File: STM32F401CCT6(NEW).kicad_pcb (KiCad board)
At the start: 2 copper layers, 37 parts, among them J1 USB_OTG, J2 Conn_02x03_Odd_Even, J3 Conn_01x20_des, J4 Conn_01x05_desc, J5 Conn_01x20, SW1 SW_Push, U1 MIC5219-3.3, U2 STM32F401CCT6, U3 USBLC6-2SC6, Y1 32.786K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

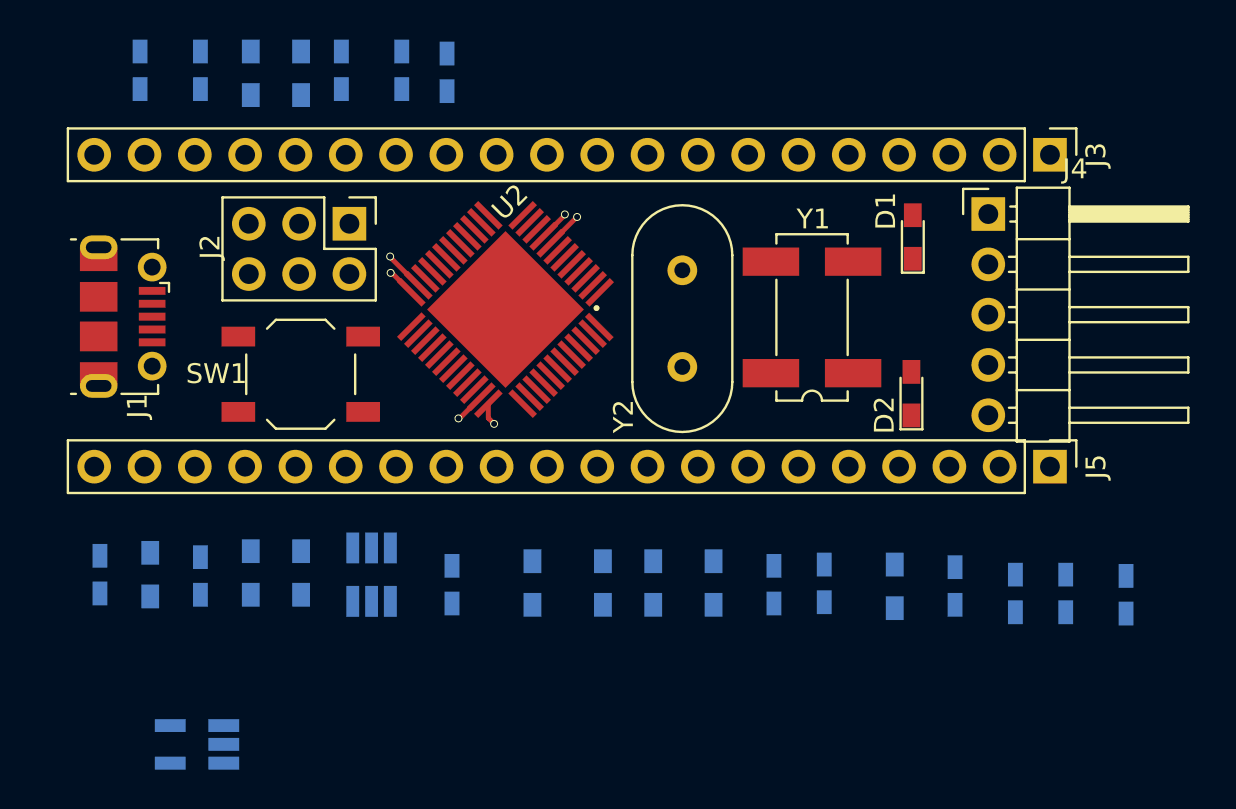
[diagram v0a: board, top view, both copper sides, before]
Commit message: Fixed QFPN48 pin 47 and 48 distances to 0.2
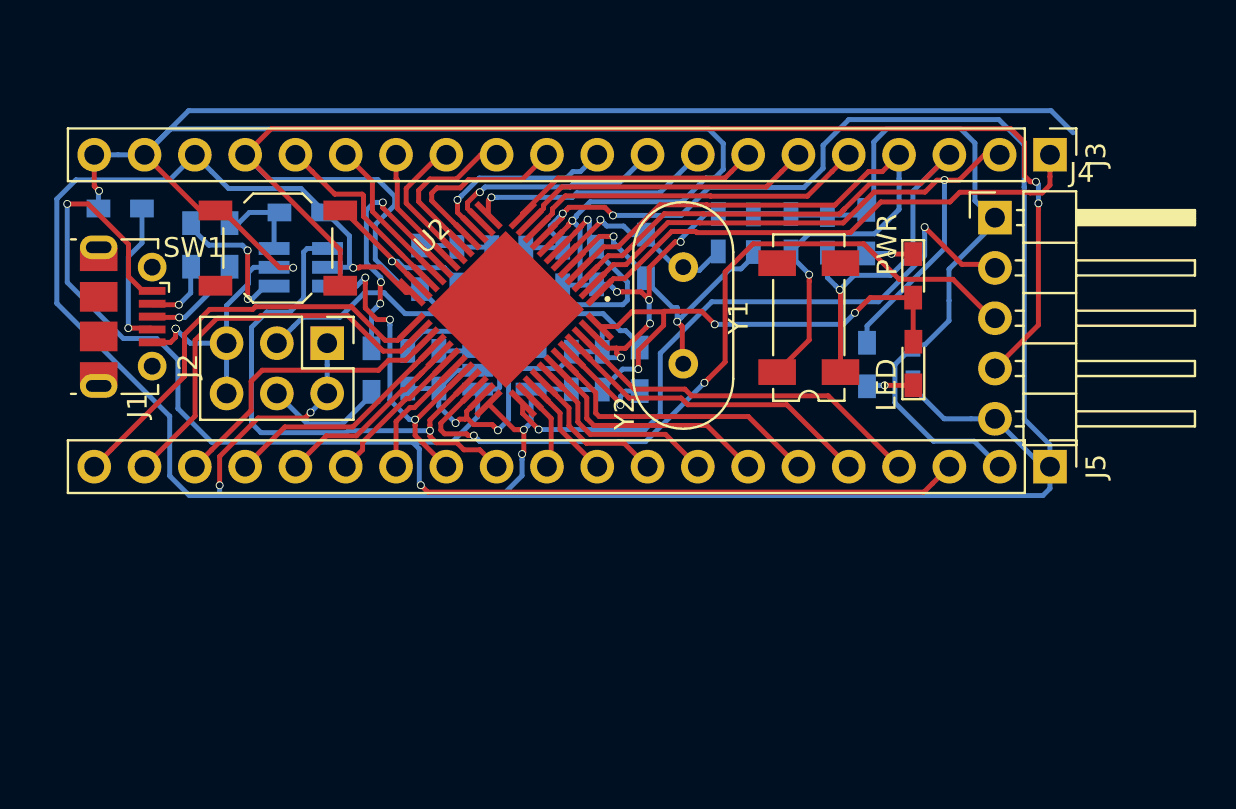
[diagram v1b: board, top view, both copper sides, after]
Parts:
- U2: footprint UFQFPN48:UFQFPN48 -> QFPN48:UFQFPN48
- Y1: footprint Crystals:Crystal_SMD_SeikoEpson_MC306-4pin_8.0x3.2mm_HandSoldering -> Crystals:Crystal_SMD_SeikoEpson_MC306-4pin_8.0x3.2mm
- moved C14 42.4 mm to (117.4, 114.2), turned to 90 degrees
- moved R6 34.4 mm to (115.1, 114.2)
- moved C2 32.7 mm to (91.9, 114.5)
- moved C8 32.0 mm to (109.3, 107.6)
- moved R5 29.6 mm to (115.0, 107.5), turned to 270 degrees
- moved R10 28.0 mm to (86.5, 106.5), turned to 0 degrees
- moved C9 27.4 mm to (107.6, 107.6), turned to 90 degrees
- moved R4 27.4 mm to (82.9, 108.2)
- moved C4 26.0 mm to (101.7, 114.5)
- moved C3 25.4 mm to (101.4, 109.2), turned to 270 degrees
- moved U1 24.4 mm to (96.8, 114.5), turned to 0 degrees
- moved C6 23.7 mm to (113.1, 107.6), turned to 90 degrees
- moved C5 22.2 mm to (100.2, 114.5), turned to 90 degrees
- moved C7 21.3 mm to (111.2, 107.6)
- moved R2 20.9 mm to (103.9, 108.8)
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- renumbered D2 to LED, D1 to PWR
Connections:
- C14 pad 1: +5V -> VCC
- J4 pad 5: +5V -> VCC
- R6 pad 1: GND -> /PC13
- Y1 pad 2: /PC15 -> (no net)
- Y1 pad 4: (no net) -> /PC15
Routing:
- net GND: track 5.54 -> 214.9 mm, vias 3 -> 13
- net VCC: track 4.14 -> 199.3 mm, vias 3 -> 10
- net /RESET: track 0.00 -> 94.6 mm, vias 0 -> 3
- net +5V: track 0.00 -> 74.6 mm, vias 0 -> 2
- net /SWDIO: track 0.00 -> 39.0 mm, vias 0 -> 2
- net /PC14: track 0.00 -> 38.1 mm, vias 0 -> 1
- net /PC15: track 0.00 -> 35.6 mm, vias 0 -> 1
- net /PC13: track 0.00 -> 33.1 mm, vias 0 -> 1
- net /SWDCLK: track 0.00 -> 32.0 mm, vias 0 -> 2
- net /PA12: track 0.00 -> 28.4 mm, vias 0 -> 1
- net /VBAT: track 0.00 -> 26.6 mm
- net /PB12: track 0.00 -> 21.6 mm
- net Net-(J2-Pad3): track 0.00 -> 20.6 mm
- net /PB13: track 0.00 -> 20.3 mm
- net /PB9: track 0.00 -> 18.5 mm
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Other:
- net class Default: clearance 0.2 -> 0.19999
- net class new: clearance 0.2 -> 0.19999
- rule trace_clearance: 0.2 -> 0.19999

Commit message: Finish routing
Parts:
- removed the LED at (117.4, 114.2)
- removed the PWR at (117.4, 109.7)
- added LED: LED_ALT, LEDs:LED_0805_HandSoldering, F.Cu at (117.4, 114.1)
- added PWR: LED_ALT, LEDs:LED_0805_HandSoldering, F.Cu at (117.4, 108.6)
- moved J4 0.34 mm to (121.5, 106.5)
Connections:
- J1 pad 6: Net-(J1-Pad6) -> (no net)
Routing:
- net GND: track 214.9 -> 165.5 mm
- net VCC: track 199.3 -> 201.6 mm
- net Net-(D1-Pad1): track 2.42 -> 3.27 mm
- net /PC13: track 33.1 -> 33.9 mm
- added copper zone on B.Cu, net GND
- added copper zone on F.Cu, net GND
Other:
- board outline added: 52.8 x 22.1 mm
- board text added: "5V"
- board text added: "A0"
- board text added: "A1"
- board text added: "A10"
- board text added: "A11"
- board text added: "A12"
- board text added: "A15"
- board text added: "A2"
- board text added: "A3"
- board text added: "A4"
- board text added: "A5"
- board text added: "A6"
- board text added: "A7"
- board text added: "A8"
- board text added: "A9"
- board text added: "B0"
- board text added: "B1"
- board text added: "B10"
- board text added: "B11"
- board text added: "B12"
- board text added: "B13"
- board text added: "B14"
- board text added: "B15"
- board text added: "B3"
- board text added: "B4"
- board text added: "B5"
- board text added: "B6"
- board text added: "B7"
- board text added: "B8"
- board text added: "B9"
- board text added: "C13"
- board text added: "C14"
- board text added: "C15"
- board text added: "GND"
- board text added: "RST"
- board text added: "SWDCLK"
- board text added: "SWDIO"
- board text added: "VB"
- board text added: "VCC"

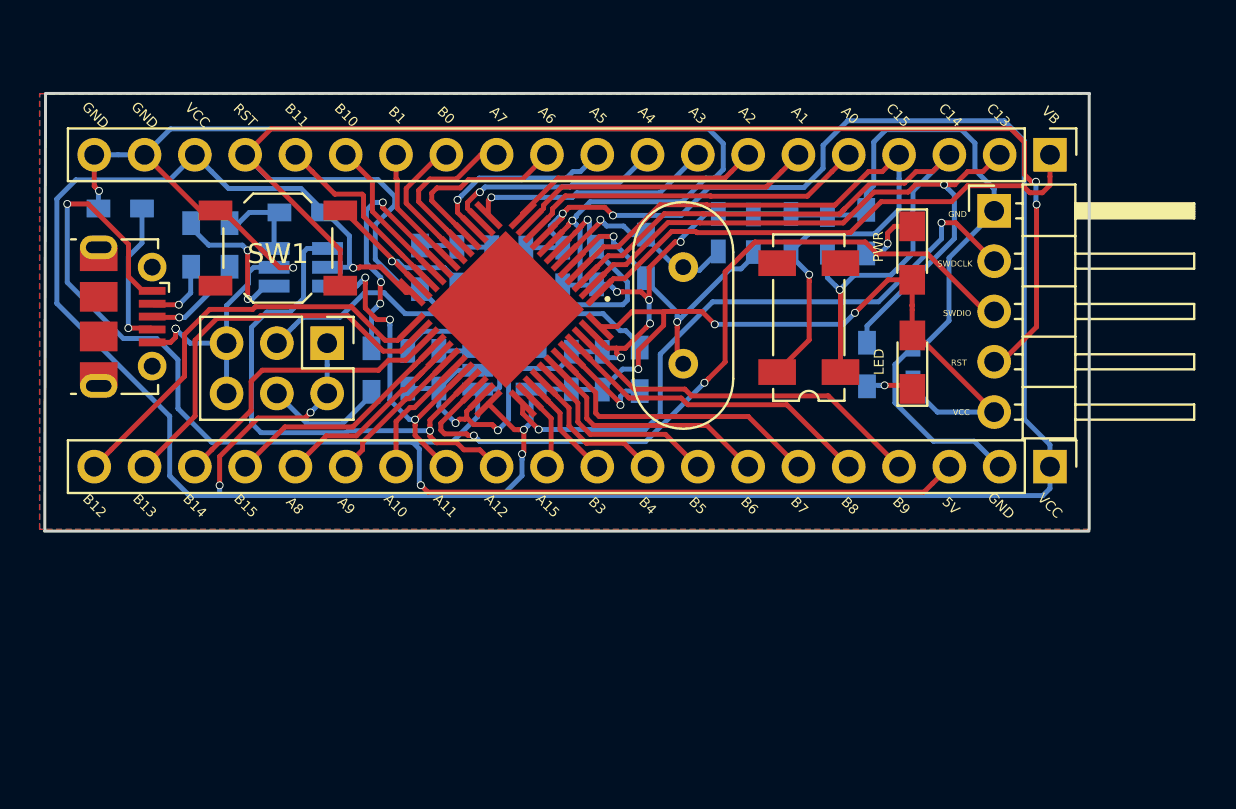
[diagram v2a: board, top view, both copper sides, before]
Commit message: Added pin name on silk layer
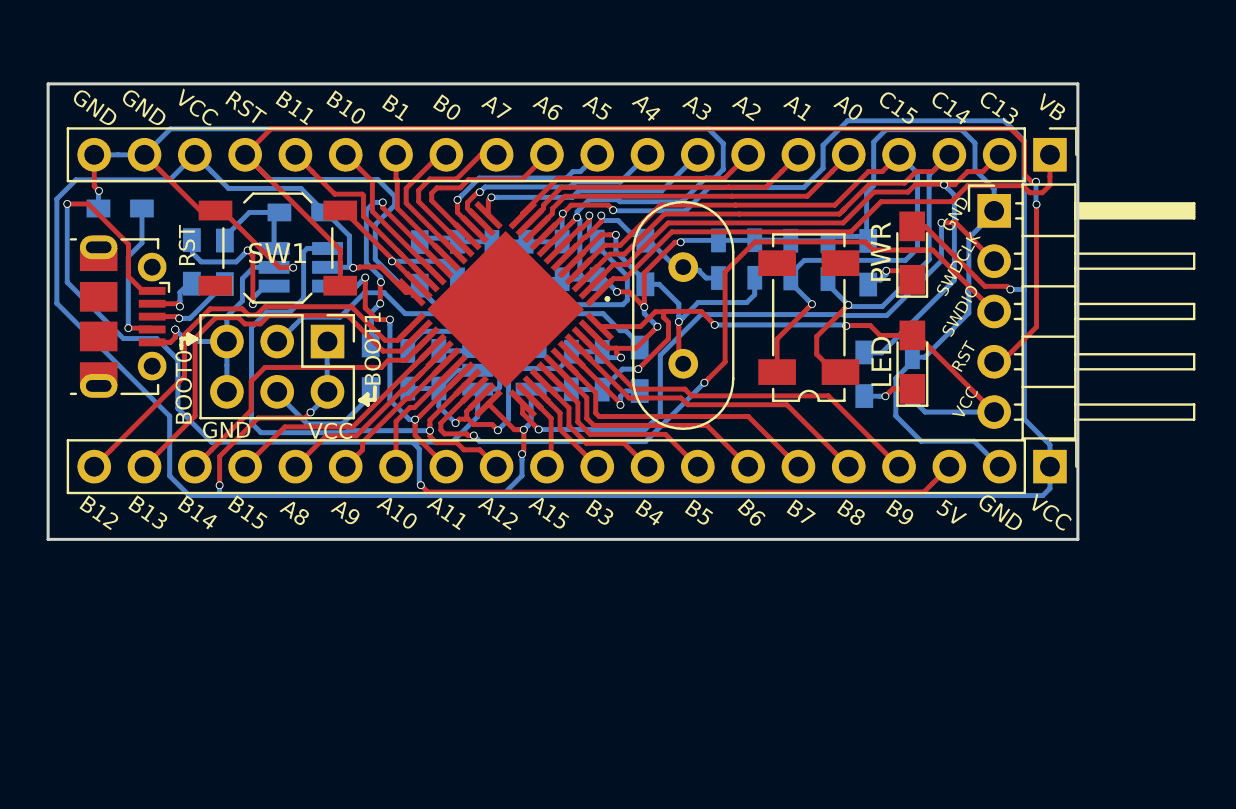
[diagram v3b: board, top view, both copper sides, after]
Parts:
- moved R5 1.57 mm to (115.1, 109.1)
- moved C7 1.36 mm to (111.2, 108.9)
- moved C9 1.34 mm to (107.6, 108.9)
- moved C6 1.33 mm to (113.1, 109.0)
- moved C8 1.30 mm to (109.4, 108.9)
- moved R4 0.91 mm to (82.7, 109.1)
- moved R3 0.86 mm to (81.0, 109.0)
- moved C14 0.63 mm to (117.4, 114.8)
- moved R6 0.51 mm to (114.9, 114.7)
- moved R2 0.31 mm to (103.9, 109.1)
- moved C11 0.31 mm to (99.7, 109.0)
- moved C10 0.29 mm to (97.9, 109.0)
- moved C3 0.26 mm to (101.5, 109.0)
- moved C12 0.26 mm to (94.4, 109.0)
- moved C13 0.26 mm to (96.1, 109.0)
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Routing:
- net GND: track 165.5 -> 168.4 mm
- net VCC: track 201.6 -> 204.5 mm, vias 10 -> 11
- net /PC15: track 35.6 -> 37.5 mm
- net /SWDIO: track 39.1 -> 41.0 mm
- net Net-(R3-Pad1): track 7.56 -> 8.51 mm
- net /PC13: track 33.9 -> 34.8 mm
- net /PC14: track 38.1 -> 38.8 mm
- net /SWDCLK: track 32.3 -> 32.9 mm
- net /OSCIN: track 16.8 -> 17.3 mm
- net /RESET: track 94.5 -> 95.0 mm
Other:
- board size 52.8 x 22.1 mm -> 52 x 23 mm
- board text added: "BOOT0"
- board text added: "BOOT1"

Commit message: Finish design the layout-Added Image on it
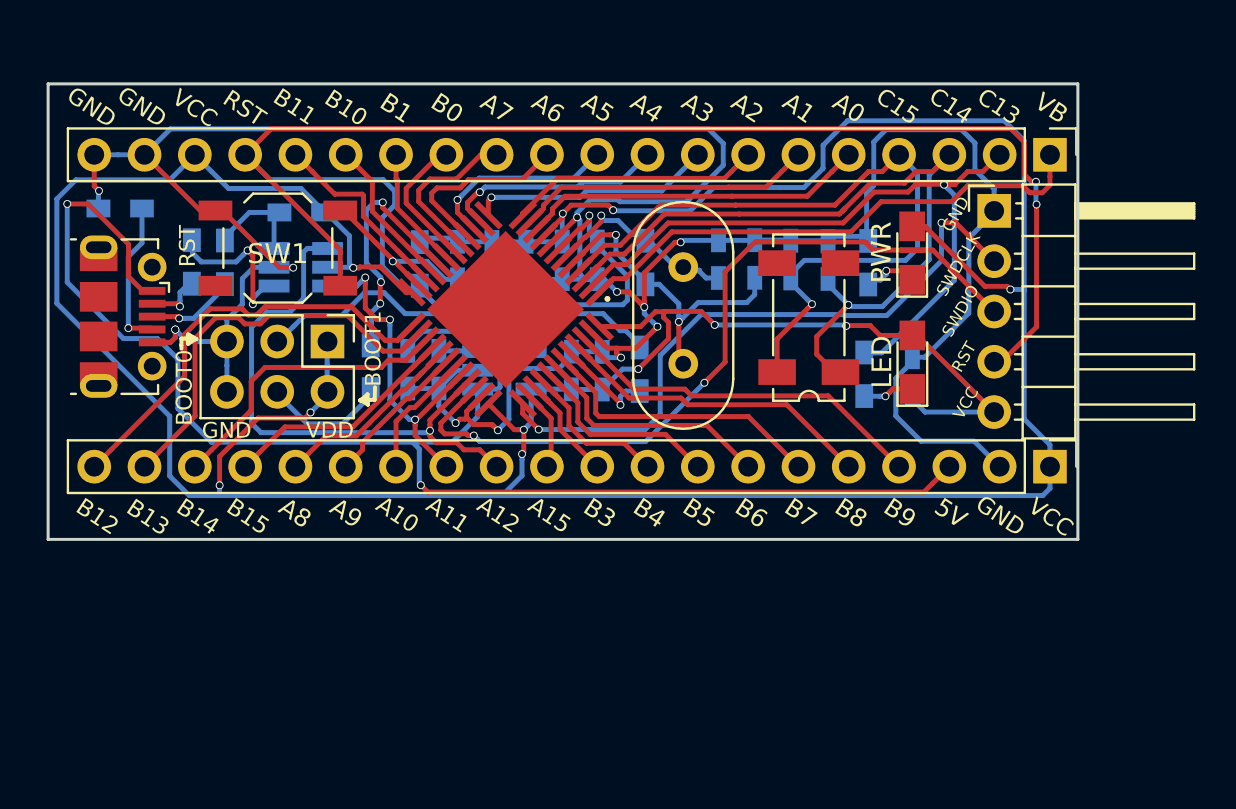
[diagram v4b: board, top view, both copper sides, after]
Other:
- board text added: "STM32F103C8T6"
- board text added: "VDD"

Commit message: Changed footprint from handsoldering to none
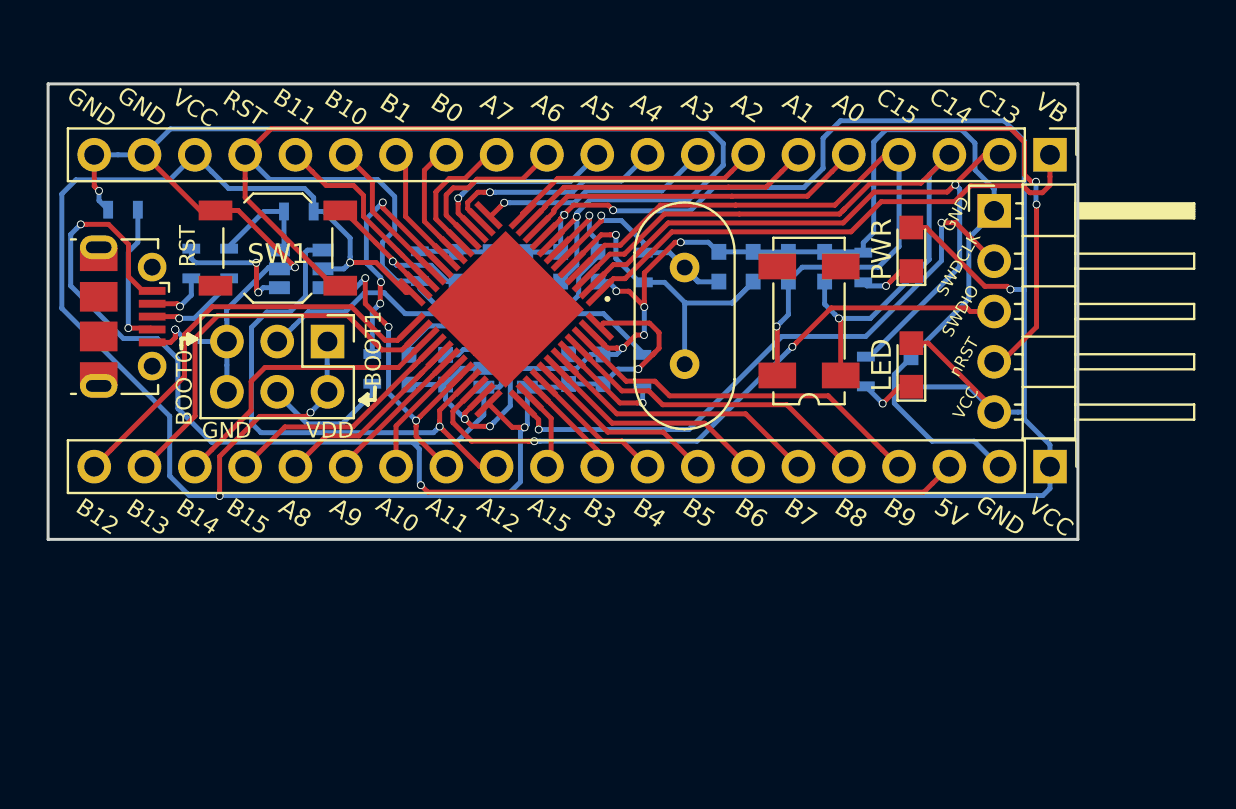
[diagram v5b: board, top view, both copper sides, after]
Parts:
- removed the LED at (117.4, 114.1)
- removed the PWR at (117.4, 108.6)
- added LED: LED_ALT, LEDs:LED_0805, F.Cu at (117.3, 114.2)
- added PWR: LED_ALT, LEDs:LED_0805, F.Cu at (117.3, 108.4)
- C1, C10, C11, C12, C13, C14, C2, C3, C4, C5, C6, C7, C8, C9: footprint Capacitors_SMD:C_0603_HandSoldering -> Capacitors_SMD:C_0603
- R1, R10, R2, R3, R4, R5, R6, R7, R8, R9: footprint Resistors_SMD:R_0603_HandSoldering -> Resistors_SMD:R_0603
- U1: footprint TO_SOT_Packages_SMD:SOT-23-5_HandSoldering -> TO_SOT_Packages_SMD:SOT-23-5
- U3: footprint TO_SOT_Packages_SMD:SOT-23-6_Handsoldering -> TO_SOT_Packages_SMD:SOT-23-6
- moved C8 0.40 mm to (109.3, 109.3)
- moved C9 0.38 mm to (107.6, 109.3)
- moved C7 0.38 mm to (111.1, 109.3)
- moved C6 0.37 mm to (112.9, 109.3)
- moved R5 0.35 mm to (114.9, 109.3)
- moved C1 0.34 mm to (93.8, 114.5)
- moved C11 0.33 mm to (99.6, 109.3)
- moved C13 0.32 mm to (96.0, 109.3)
- moved C3 0.32 mm to (101.5, 109.3)
- moved C10 0.32 mm to (97.8, 109.3)
- moved C12 0.32 mm to (94.3, 109.3)
- moved R2 0.26 mm to (103.8, 109.3)
- moved R4 0.22 mm to (82.9, 109.1)
- moved C14 0.21 mm to (117.3, 114.6)
- moved Y1 0.17 mm to (112.2, 112.0)
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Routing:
- net VCC: track 204.5 -> 192.5 mm, vias 11 -> 8
- net /SWDIO: track 41.0 -> 33.4 mm
- net GND: track 168.2 -> 163.1 mm
- net /RESET: track 94.9 -> 92.1 mm
- net +5V: track 74.7 -> 72.1 mm
- net /PC15: track 37.5 -> 35.3 mm
- net Net-(R3-Pad1): track 8.51 -> 6.57 mm
- net /SWDCLK: track 32.9 -> 31.2 mm
- net /PA7: track 8.23 -> 6.95 mm
- net /OSCOUT: track 10.5 -> 11.7 mm
- net /PA6: track 9.55 -> 8.46 mm
- net /PB0: track 6.84 -> 6.08 mm
- net /PA12: track 28.4 -> 27.7 mm
- net Net-(R10-Pad1): track 5.09 -> 5.71 mm
- net Net-(C2-Pad1): track 7.19 -> 7.80 mm
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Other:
- board text added: "nRST"
- board text removed: "STM32F103C8T6"
